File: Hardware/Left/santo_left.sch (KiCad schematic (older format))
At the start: 11 parts, among them J1 USB_C_Receptacle, J2 USB_C_Receptacle, U1 ATMEGA32U4-MU

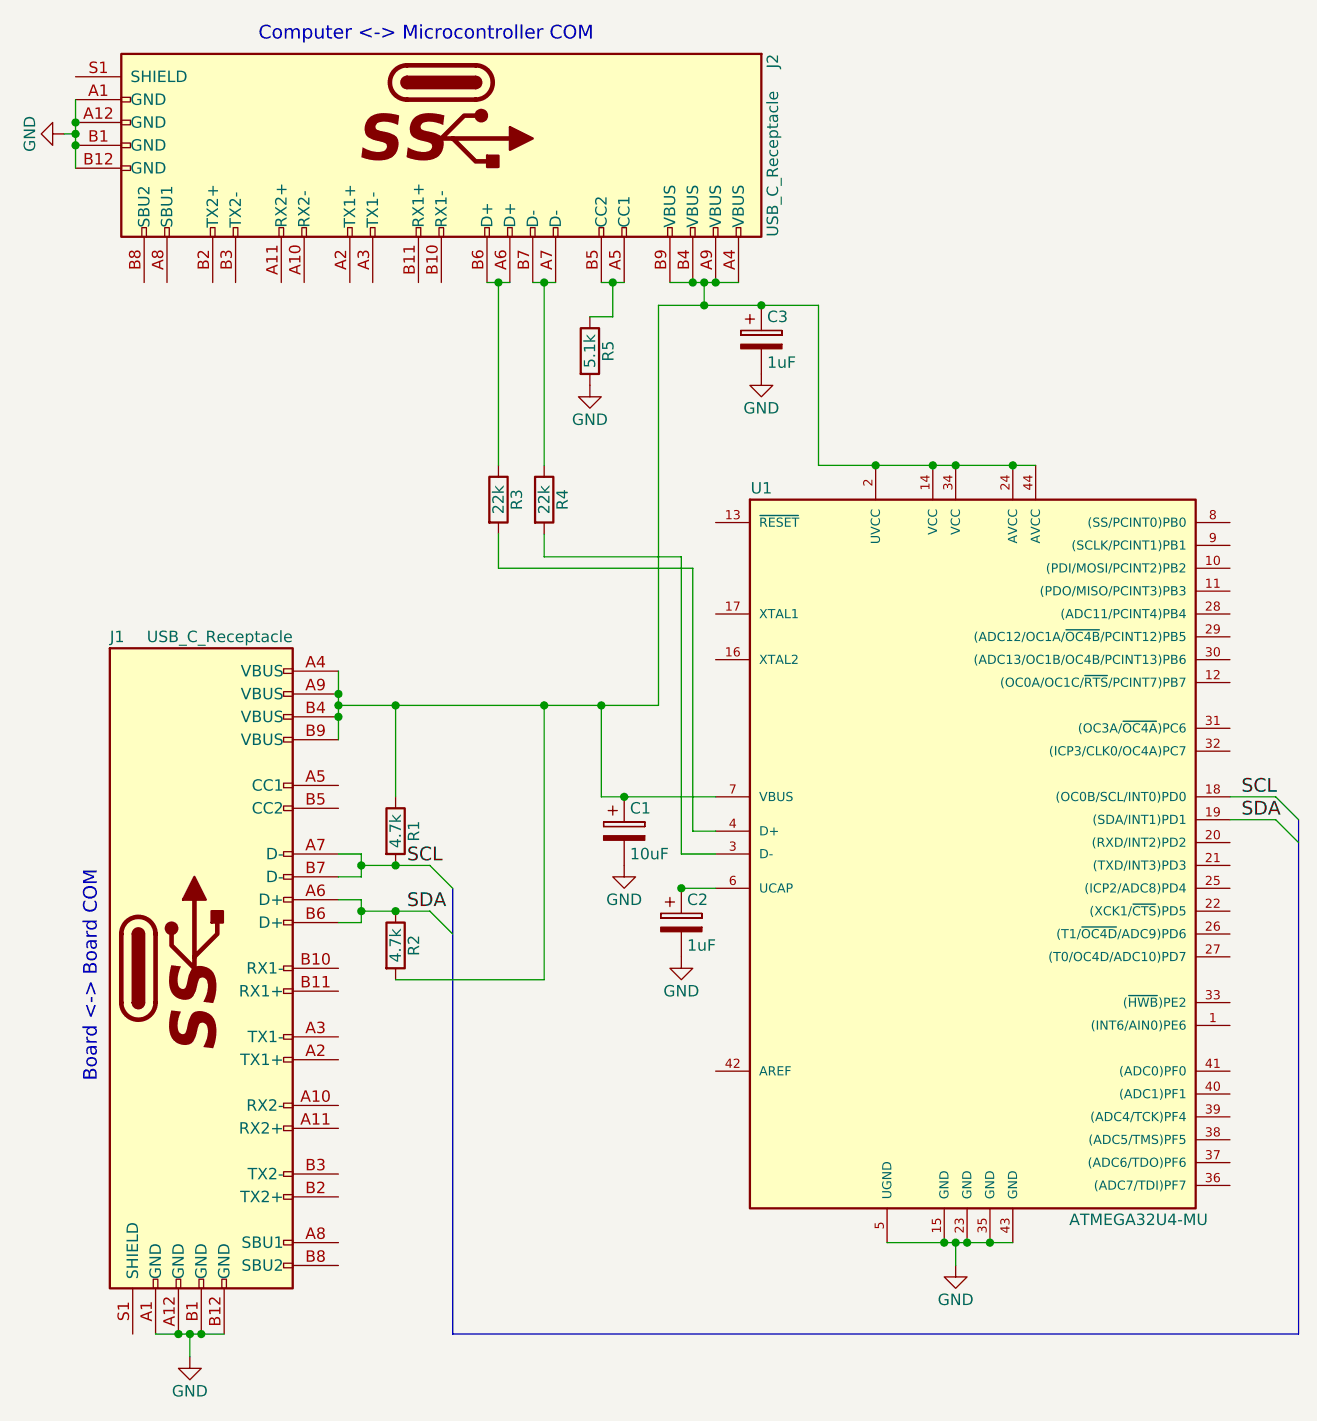
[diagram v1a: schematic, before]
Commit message: Wire up reset.
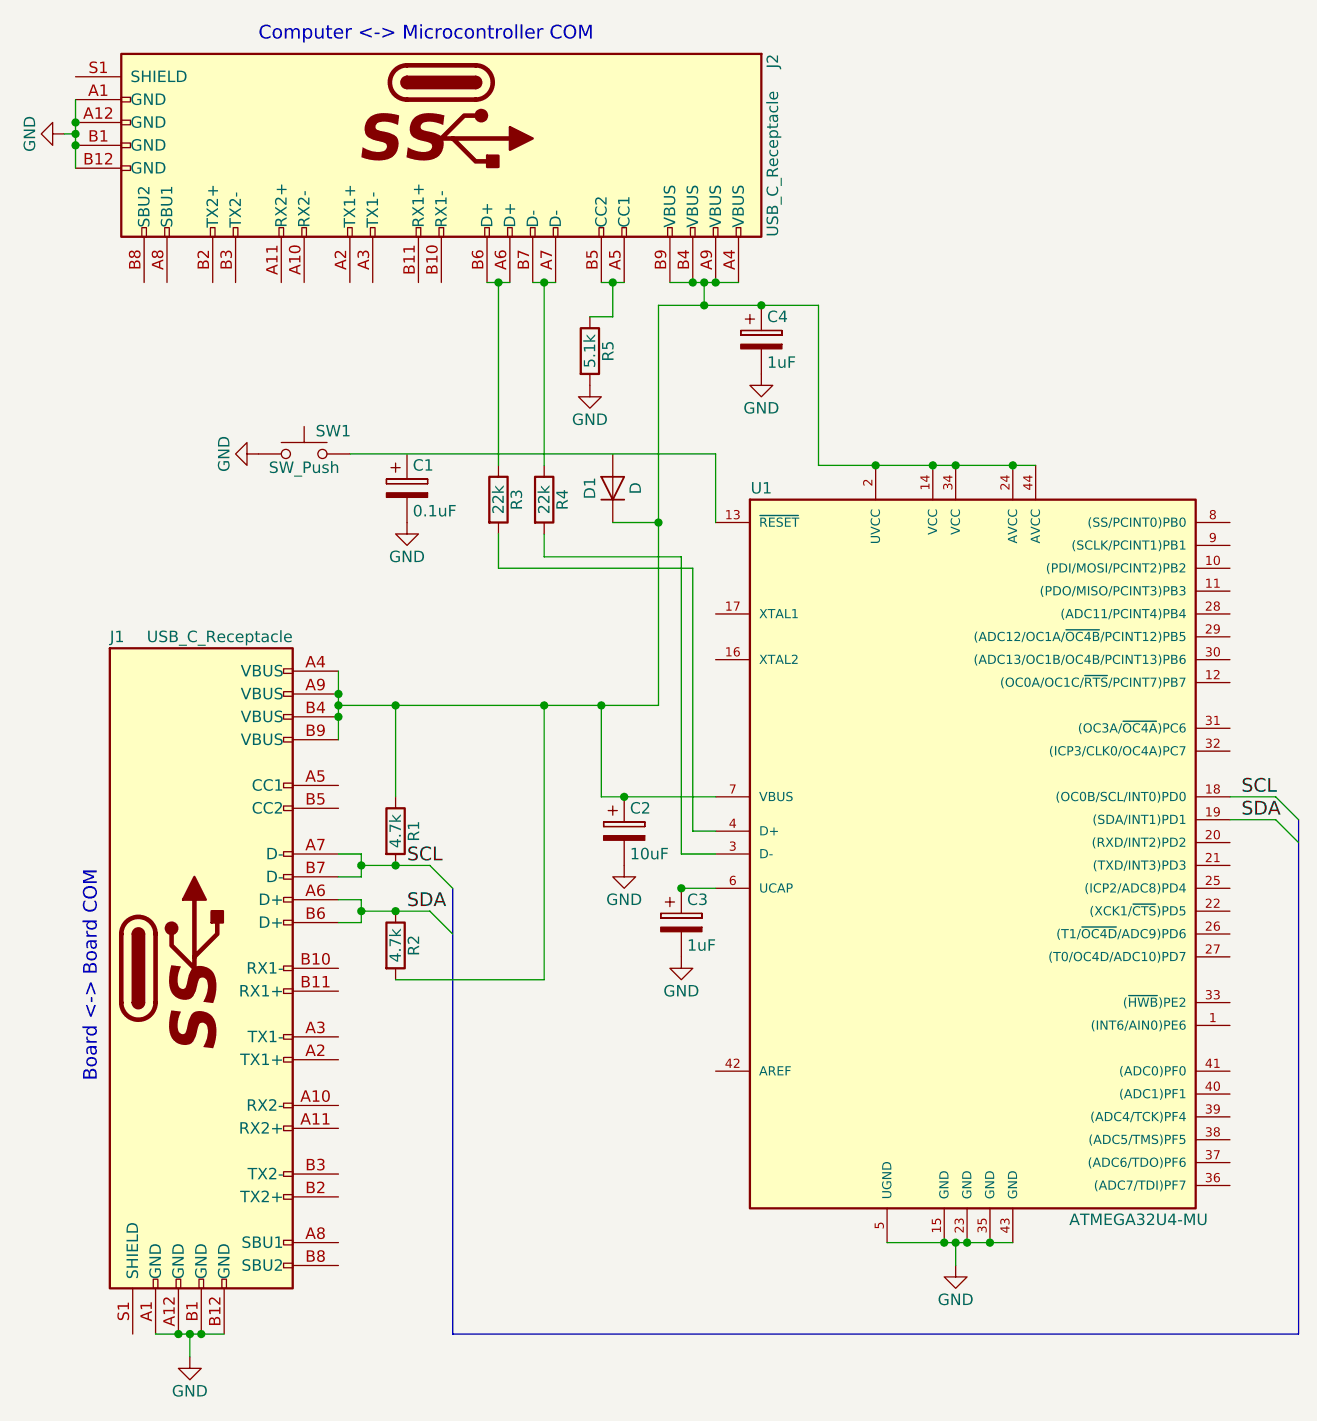
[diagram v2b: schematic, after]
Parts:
- added C1: 0.1uF, symbol CP
- added D1: D, symbol D
- added SW1: SW_Push, symbol SW_Push
- renumbered C1 to C2, C2 to C3, C3 to C4
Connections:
- net GND: now also C1.2, SW1.1
- net at U1.13 (~RESET~): now also SW1.2
- net at C2.1, C4.1, J1.A4 (VBUS)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: now also D1.1 (K)
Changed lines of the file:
@@
 $EndComp
 $Comp
-L CP C2
+L CP C3
 U 1 1 5A092A38
 P 3400 4500
-F 0 "C2" H 3425 4600 50  0000 L CNN
+F 0 "C3" H 3425 4600 50  0000 L CNN
 F 1 "1uF" H 3425 4400 50  0000 L CNN
 F 2 "" H 3438 4350 50  0001 C CNN
@@
 $EndComp
 $Comp
-L GND #PWR5
+L GND #PWR7
 U 1 1 5A092A79
 P 3400 4650
-F 0 "#PWR5" H 3400 4400 50  0001 C CNN
+F 0 "#PWR7" H 3400 4400 50  0001 C CNN
 F 1 "GND" H 3400 4500 50  0000 C CNN
 F 2 "" H 3400 4650 50  0001 C CNN
@@
 $EndComp
 $Comp
-L CP C1
+L CP C2
 U 1 1 5A0933EF
 P 3150 4100
-F 0 "C1" H 3175 4200 50  0000 L CNN
+F 0 "C2" H 3175 4200 50  0000 L CNN
 F 1 "10uF" H 3175 4000 50  0000 L CNN
 F 2 "" H 3188 3950 50  0001 C CNN
@@
 $EndComp
 $Comp
-L GND #PWR4
+L GND #PWR6
 U 1 1 5A09341E
 P 3150 4250
-F 0 "#PWR4" H 3150 4000 50  0001 C CNN
+F 0 "#PWR6" H 3150 4000 50  0001 C CNN
 F 1 "GND" H 3150 4100 50  0000 C CNN
 F 2 "" H 3150 4250 50  0001 C CNN
@@
 $EndComp
 $Comp
-L GND #PWR7
+L GND #PWR9
 U 1 1 5A093698
 P 4600 6000
-F 0 "#PWR7" H 4600 5750 50  0001 C CNN
+F 0 "#PWR9" H 4600 5750 50  0001 C CNN
 F 1 "GND" H 4600 5850 50  0000 C CNN
 F 2 "" H 4600 6000 50  0001 C CNN
@@
 SDA
 $Comp
-L CP C3
+L CP C4
 U 1 1 5A094C59
 P 3750 1950
-F 0 "C3" H 3775 2050 50  0000 L CNN
+F 0 "C4" H 3775 2050 50  0000 L CNN
 F 1 "1uF" H 3775 1850 50  0000 L CNN
 F 2 "" H 3788 1800 50  0001 C CNN
@@
 $EndComp
 $Comp
-L GND #PWR6
+L GND #PWR8
 U 1 1 5A094E64
 P 3750 2100
-F 0 "#PWR6" H 3750 1850 50  0001 C CNN
+F 0 "#PWR8" H 3750 1850 50  0001 C CNN
 F 1 "GND" H 3750 1950 50  0000 C CNN
 F 2 "" H 3750 2100 50  0001 C CNN
@@
 $EndComp
 $Comp
-L GND #PWR3
+L GND #PWR5
 U 1 1 5A095FF2
 P 3000 2150
-F 0 "#PWR3" H 3000 1900 50  0001 C CNN
+F 0 "#PWR5" H 3000 1900 50  0001 C CNN
 F 1 "GND" H 3000 2000 50  0000 C CNN
 F 2 "" H 3000 2150 50  0001 C CNN
@@
 Wire Wire Line
 	2800 2900 2800 2800
+Wire Wire Line
+	3550 2750 3550 2450
+Wire Wire Line
+	3550 2450 1950 2450
+$Comp
+L CP C1
+U 1 1 5A0975BA
+P 2200 2600
+F 0 "C1" H 2225 2700 50  0000 L CNN
+F 1 "0.1uF" H 2225 2500 50  0000 L CNN
+F 2 "" H 2238 2450 50  0001 C CNN
+F 3 "" H 2200 2600 50  0001 C CNN
+	1    2200 2600
+	1    0    0    -1
+$EndComp
+$Comp
+L GND #PWR4
+U 1 1 5A097643
+P 2200 2750
+F 0 "#PWR4" H 2200 2500 50  0001 C CNN
+F 1 "GND" H 2200 2600 50  0000 C CNN
+F 2 "" H 2200 2750 50  0001 C CNN
+F 3 "" H 2200 2750 50  0001 C CNN
+	1    2200 2750
+	1    0    0    -1
+$EndComp
+$Comp
+L SW_Push SW1
+U 1 1 5A0976B7
+P 1750 2450
+F 0 "SW1" H 1800 2550 50  0000 L CNN
+F 1 "SW_Push" H 1750 2390 50  0000 C CNN
+F 2 "" H 1750 2650 50  0001 C CNN
+F 3 "" H 1750 2650 50  0001 C CNN
+	1    1750 2450
+	1    0    0    -1
+$EndComp
+$Comp
+L GND #PWR3
+U 1 1 5A097729
+P 1550 2450
+F 0 "#PWR3" H 1550 2200 50  0001 C CNN
+F 1 "GND" H 1550 2300 50  0000 C CNN
+F 2 "" H 1550 2450 50  0001 C CNN
+F 3 "" H 1550 2450 50  0001 C CNN
+	1    1550 2450
+	0    1    1    0
+$EndComp
+$Comp
+L D D1
+U 1 1 5A097777
+P 3100 2600
+F 0 "D1" H 3100 2700 50  0000 C CNN
+F 1 "D" H 3100 2500 50  0000 C CNN
+F 2 "" H 3100 2600 50  0001 C CNN
+F 3 "" H 3100 2600 50  0001 C CNN
+	1    3100 2600
+	0    -1   -1   0
+$EndComp
+Wire Wire Line
+	3100 2750 3300 2750
+Connection ~ 3300 2750
 $EndSCHEMATC
